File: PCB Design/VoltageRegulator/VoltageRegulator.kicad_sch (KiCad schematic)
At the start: 31 parts, among them J1 Screw_Terminal_01x08, J2 SMA, J3 SMA, J4 SMA, J5 SMA, J6 SMA, J7 SMA, J8 Screw_Terminal_01x01, U1 LM7815_TO220, U2 L7805, U3 ADL5902ACPZ-R7, U4 LM358

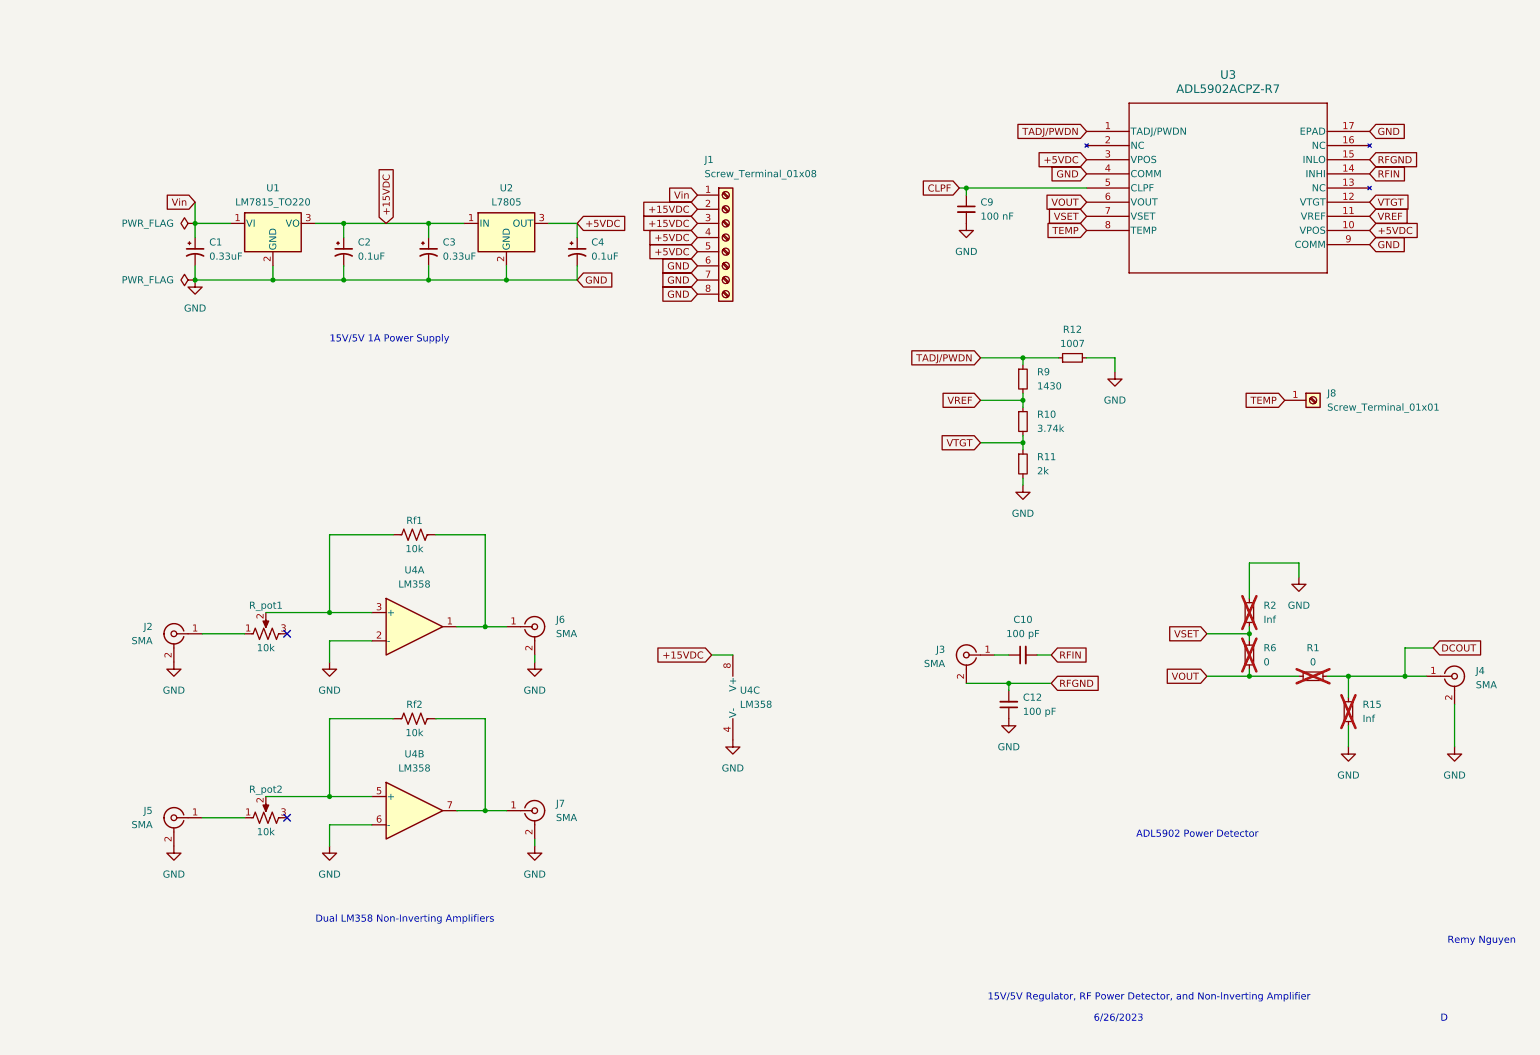
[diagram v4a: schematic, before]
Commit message: New circuit diagram  with current draw
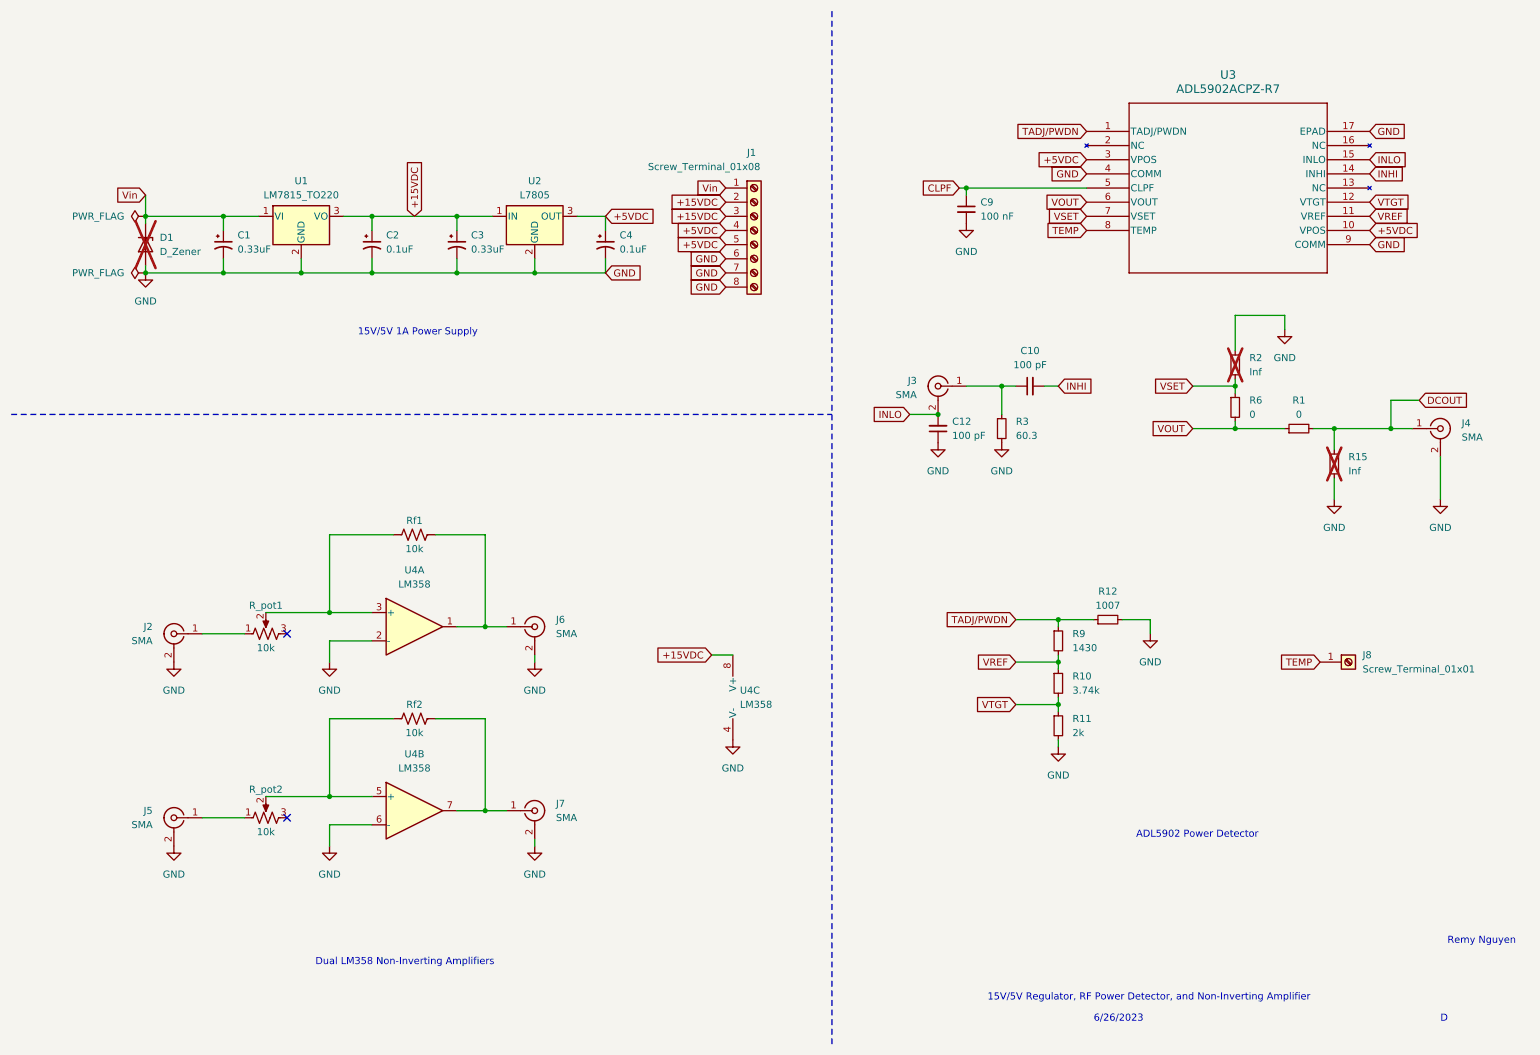
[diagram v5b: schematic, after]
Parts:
- added D1: D_Zener, symbol Device:D_Zener
- added R3: 60.3, symbol Device:R_Small
- R1, R6: now fitted
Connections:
- net GND: now also D1.2 (A), R3.2
- net Vin: now also D1.1 (K)
- net at C10.1, J3.1 (In): now also R3.1
- net RFGND renamed INLO
- net RFIN renamed INHI
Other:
- moved on the sheet: C1, C10, C12, C2, C3, C4, J1, J3, J4, J8, R10, R11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

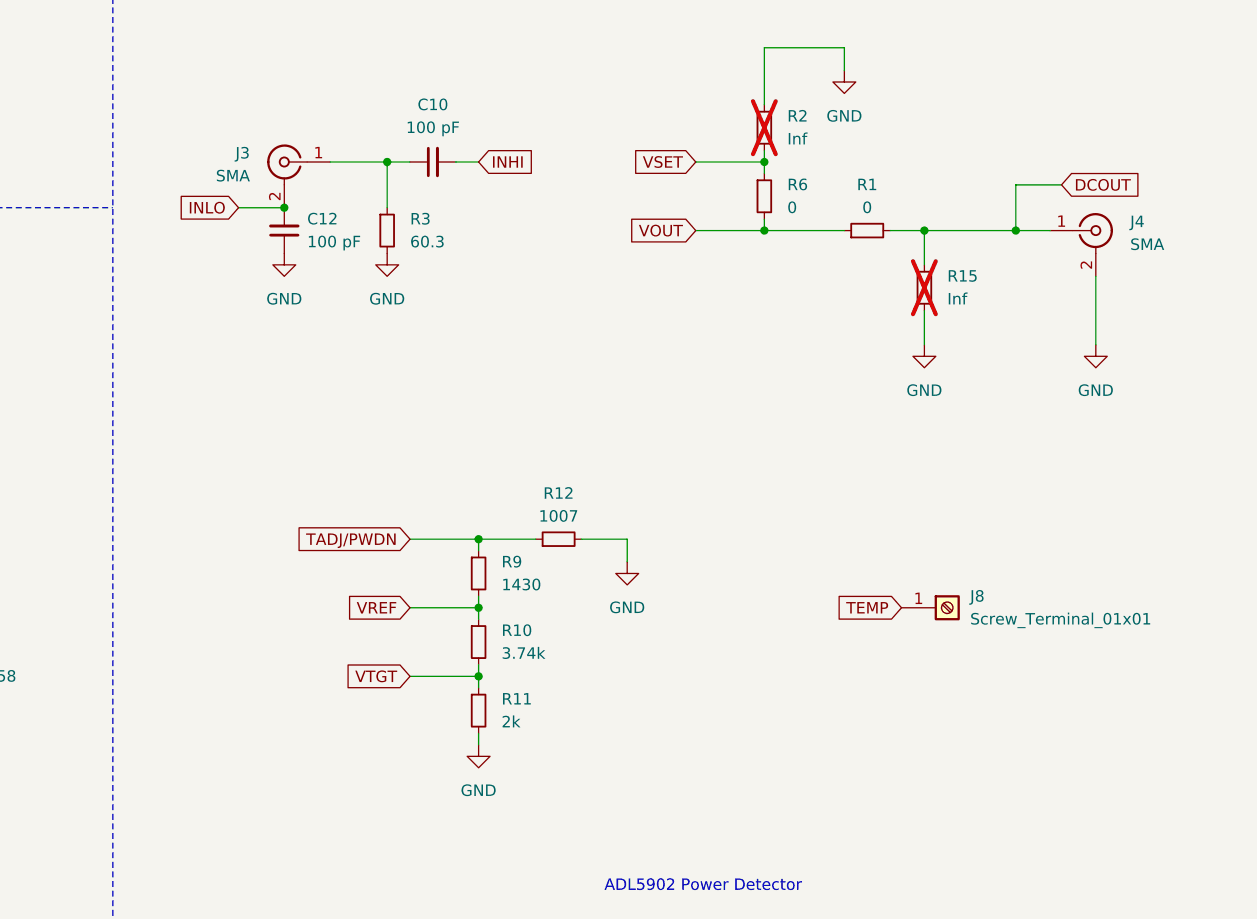
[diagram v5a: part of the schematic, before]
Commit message: INLO fixed; INLO is unused differential input, not RFGND
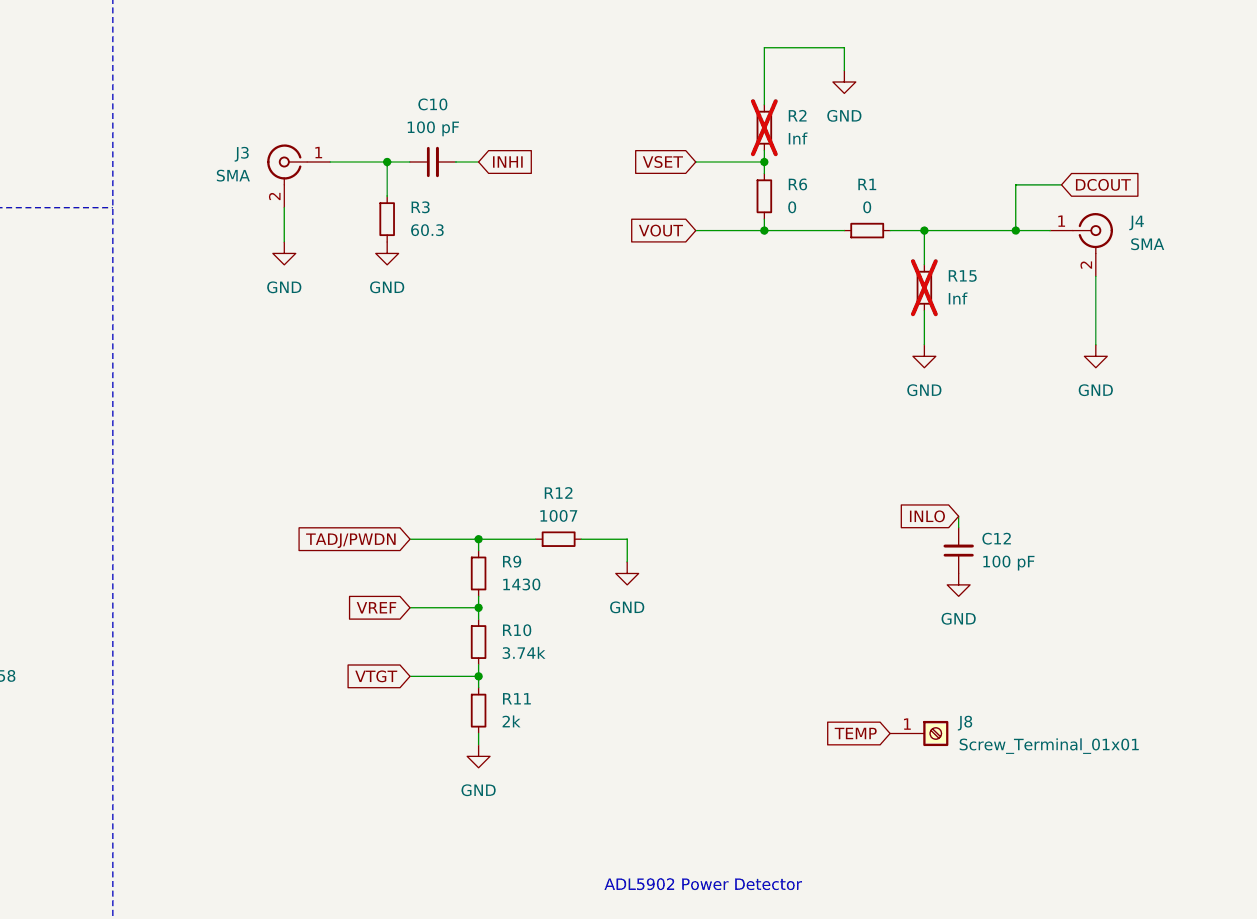
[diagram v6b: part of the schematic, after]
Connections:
- net GND: now also J3.2 (Ext)
- net INLO: no longer J3.2 (Ext)
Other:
- moved on the sheet: C12, J8, R3
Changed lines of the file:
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@@
   (junction (at 232.41 87.63) (diameter 0) (color 0 0 0 0)
-  )
-  (junction (at 179.07 85.09) (diameter 0) (color 0 0 0 0)
   )
   (junction (at 200.66 137.16) (diameter 0) (color 0 0 0 0)
@@
     (stroke (width 0) (type default))
   )
+  (wire (pts (xy 179.07 85.09) (xy 179.07 88.9))
+    (stroke (width 0) (type default))
+  )
   (wire (pts (xy 97.79 139.7) (xy 88.9 139.7))
     (stroke (width 0) (type default))
@@
     (stroke (width 0) (type default))
   )
-  (wire (pts (xy 190.5 80.01) (xy 190.5 85.09))
+  (wire (pts (xy 190.5 80.01) (xy 190.5 83.82))
     (stroke (width 0) (type default))
   )
@@
     (stroke (width 0) (type default))
   )
-  (wire (pts (xy 173.99 85.09) (xy 179.07 85.09))
+  (wire (pts (xy 254 119.38) (xy 254 120.65))
     (stroke (width 0) (type default))
   )
@@
     )
   )
-  (global_label "INLO" (shape input) (at 173.99 85.09 180) (fields_autoplaced)
-    (effects (font (size 1.27 1.27)) (justify right))
-    (property "Intersheetrefs" "${INTERSHEET_REFS}" (at 166.7903 85.09 0)
+  (global_label "INLO" (shape input) (at 254 119.38 180) (fields_autoplaced)
+    (effects (font (size 1.27 1.27)) (justify right))
+    (property "Intersheetrefs" "${INTERSHEET_REFS}" (at 246.8003 119.38 0)
       (effects (font (size 1.27 1.27)) (justify right) hide)
     )
@@
     )
   )
-  (global_label "TEMP" (shape input) (at 247.65 129.54 180) (fields_autoplaced)
-    (effects (font (size 1.27 1.27)) (justify right))
-    (property "Intersheetrefs" "${INTERSHEET_REFS}" (at 239.9062 129.54 0)
+  (global_label "TEMP" (shape input) (at 246.38 143.51 180) (fields_autoplaced)
+    (effects (font (size 1.27 1.27)) (justify right))
+    (property "Intersheetrefs" "${INTERSHEET_REFS}" (at 238.6362 143.51 0)
       (effects (font (size 1.27 1.27)) (justify right) hide)
     )
@@
     )
   )
-  (symbol (lib_id "Device:R_Small") (at 190.5 87.63 0) (unit 1)
-    (in_bom yes) (on_board yes) (dnp no) (fields_autoplaced)
-    (property "Reference" "R3" (at 193.04 86.36 0)
-      (effects (font (size 1.27 1.27)) (justify left))
-    )
-    (property "Value" "60.3" (at 193.04 88.9 0)
-      (effects (font (size 1.27 1.27)) (justify left))
-    )
-    (property "Footprint" "" (at 190.5 87.63 0)
-      (effects (font (size 1.27 1.27)) hide)
-    )
-    (property "Datasheet" "~" (at 190.5 87.63 0)
+  (symbol (lib_id "Device:R_Small") (at 190.5 86.36 0) (unit 1)
+    (in_bom yes) (on_board yes) (dnp no) (fields_autoplaced)
+    (property "Reference" "R3" (at 193.04 85.09 0)
+      (effects (font (size 1.27 1.27)) (justify left))
+    )
+    (property "Value" "60.3" (at 193.04 87.63 0)
+      (effects (font (size 1.27 1.27)) (justify left))
+    )
+    (property "Footprint" "" (at 190.5 86.36 0)
+      (effects (font (size 1.27 1.27)) hide)
+    )
+    (property "Datasheet" "~" (at 190.5 86.36 0)
       (effects (font (size 1.27 1.27)) hide)
     )
@@
     )
   )
+  (symbol (lib_id "power:GND") (at 179.07 88.9 0) (unit 1)
+    (in_bom yes) (on_board yes) (dnp no) (fields_autoplaced)
+    (property "Reference" "#PWR03" (at 179.07 95.25 0)
+      (effects (font (size 1.27 1.27)) hide)
+    )
+    (property "Value" "GND" (at 179.07 93.98 0)
+      (effects (font (size 1.27 1.27)))
+    )
+    (property "Footprint" "" (at 179.07 88.9 0)
+      (effects (font (size 1.27 1.27)) hide)
+    )
+    (property "Datasheet" "" (at 179.07 88.9 0)
+      (effects (font (size 1.27 1.27)) hide)
+    )
+    (pin "1")
+    (instances
+      (project "VoltageRegulator"
+        (path "/0e389307-4ee7-48a5-9908-22ab90894211"
+          (reference "#PWR03") (unit 1)
+        )
+      )
+    )
+  )
   (symbol (lib_id "power:GND") (at 217.17 124.46 0) (unit 1)
     (in_bom yes) (on_board yes) (dnp no) (fields_autoplaced)
@@
     )
   )
-  (symbol (lib_id "Connector:Screw_Terminal_01x01") (at 252.73 129.54 0) (unit 1)
-    (in_bom yes) (on_board yes) (dnp no) (fields_autoplaced)
-    (property "Reference" "J8" (at 255.27 128.27 0)
-      (effects (font (size 1.27 1.27)) (justify left))
-    )
-    (property "Value" "Screw_Terminal_01x01" (at 255.27 130.81 0)
-      (effects (font (size 1.27 1.27)) (justify left))
-    )
-    (property "Footprint" "" (at 252.73 129.54 0)
-      (effects (font (size 1.27 1.27)) hide)
-    )
-    (property "Datasheet" "~" (at 252.73 129.54 0)
+  (symbol (lib_id "Connector:Screw_Terminal_01x01") (at 251.46 143.51 0) (unit 1)
+    (in_bom yes) (on_board yes) (dnp no) (fields_autoplaced)
+    (property "Reference" "J8" (at 254 142.24 0)
+      (effects (font (size 1.27 1.27)) (justify left))
+    )
+    (property "Value" "Screw_Terminal_01x01" (at 254 144.78 0)
+      (effects (font (size 1.27 1.27)) (justify left))
+    )
+    (property "Footprint" "" (at 251.46 143.51 0)
+      (effects (font (size 1.27 1.27)) hide)
+    )
+    (property "Datasheet" "~" (at 251.46 143.51 0)
       (effects (font (size 1.27 1.27)) hide)
     )
@@
     )
   )
-  (symbol (lib_id "power:GND") (at 190.5 90.17 0) (unit 1)
-    (in_bom yes) (on_board yes) (dnp no) (fields_autoplaced)
-    (property "Reference" "#PWR02" (at 190.5 96.52 0)
-      (effects (font (size 1.27 1.27)) hide)
-    )
-    (property "Value" "GND" (at 190.5 95.25 0)
-      (effects (font (size 1.27 1.27)))
-    )
-    (property "Footprint" "" (at 190.5 90.17 0)
-      (effects (font (size 1.27 1.27)) hide)
-    )
-    (property "Datasheet" "" (at 190.5 90.17 0)
+  (symbol (lib_id "power:GND") (at 190.5 88.9 0) (unit 1)
+    (in_bom yes) (on_board yes) (dnp no) (fields_autoplaced)
+    (property "Reference" "#PWR02" (at 190.5 95.25 0)
+      (effects (font (size 1.27 1.27)) hide)
+    )
+    (property "Value" "GND" (at 190.5 93.98 0)
+      (effects (font (size 1.27 1.27)))
+    )
+    (property "Footprint" "" (at 190.5 88.9 0)
+      (effects (font (size 1.27 1.27)) hide)
+    )
+    (property "Datasheet" "" (at 190.5 88.9 0)
       (effects (font (size 1.27 1.27)) hide)
     )
@@
     )
   )
-  (symbol (lib_id "power:GND") (at 179.07 90.17 0) (unit 1)
-    (in_bom yes) (on_board yes) (dnp no) (fields_autoplaced)
-    (property "Reference" "#PWR011" (at 179.07 96.52 0)
-      (effects (font (size 1.27 1.27)) hide)
-    )
-    (property "Value" "GND" (at 179.07 95.25 0)
-      (effects (font (size 1.27 1.27)))
-    )
-    (property "Footprint" "" (at 179.07 90.17 0)
-      (effects (font (size 1.27 1.27)) hide)
-    )
-    (property "Datasheet" "" (at 179.07 90.17 0)
+  (symbol (lib_id "power:GND") (at 254 125.73 0) (unit 1)
+    (in_bom yes) (on_board yes) (dnp no) (fields_autoplaced)
+    (property "Reference" "#PWR011" (at 254 132.08 0)
+      (effects (font (size 1.27 1.27)) hide)
+    )
+    (property "Value" "GND" (at 254 130.81 0)
+      (effects (font (size 1.27 1.27)))
+    )
+    (property "Footprint" "" (at 254 125.73 0)
+      (effects (font (size 1.27 1.27)) hide)
+    )
+    (property "Datasheet" "" (at 254 125.73 0)
       (effects (font (size 1.27 1.27)) hide)
     )
@@
     )
   )
-  (symbol (lib_id "Device:C_Small") (at 179.07 87.63 180) (unit 1)
-    (in_bom yes) (on_board yes) (dnp no) (fields_autoplaced)
-    (property "Reference" "C12" (at 181.61 86.3536 0)
+  (symbol (lib_id "Device:C_Small") (at 254 123.19 180) (unit 1)
+    (in_bom yes) (on_board yes) (dnp no) (fields_autoplaced)
+    (property "Reference" "C12" (at 256.54 121.9136 0)
       (effects (font (size 1.27 1.27)) (justify right))
     )
-    (property "Value" "100 pF" (at 181.61 88.8936 0)
+    (property "Value" "100 pF" (at 256.54 124.4536 0)
       (effects (font (size 1.27 1.27)) (justify right))
     )
-    (property "Footprint" "" (at 179.07 87.63 0)
-      (effects (font (size 1.27 1.27)) hide)
-    )
-    (property "Datasheet" "~" (at 179.07 87.63 0)
-      (effects (font (size 1.27 1.27)) hide)
-    )
+    (property "Footprint" "" (at 254 123.19 0)
+      (effects (font (size 1.27 1.27)) hide)
+    )
+    (property "Datasheet" "~" (at 254 123.19 0)
+      (effects (font (size 1.27 1.27)) hide)
+    )

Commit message: Footprints assigned, LM7815 --> L7815
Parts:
- C1, C2, C3, C4: footprint Capacitor_THT:CP_Radial_Tantal_D4.5mm_P2.50mm -> Capacitor_Tantalum_SMD:CP_EIA-1608-08_AVX-J
- C10, C12: footprint (none) -> Capacitor_SMD:C_1206_3216Metric
- C9: footprint (none) -> Capacitor_SMD:C_0805_2012Metric
- D1: footprint (none) -> Diode_SMD:D_1206_3216Metric
- J2, J3, J4, J5, J6, J7: footprint (none) -> Connector_Coaxial:SMA_Molex_73251-1153_EdgeMount_Horizontal
- J8: value Screw_Terminal_01x01 -> Conn_01x01; footprint (none) -> Connector_PinHeader_1.00mm:PinHeader_1x01_P1.00mm_Vertical; symbol Connector:Screw_Terminal_01x01 -> Connector_Generic:Conn_01x01; now not fitted
- R1, R12, R15, R2, R6, R9, Rf1, Rf2: footprint (none) -> Resistor_SMD:R_1206_3216Metric
- R10, R11, R3: footprint (none) -> Resistor_SMD:R_0805_2012Metric
- R_pot1, R_pot2: footprint (none) -> Potentiometer_THT:Potentiometer_Bourns_3006P_Horizontal
- U1: value LM7815_TO220 -> L7815; symbol Regulator_Linear:LM7815_TO220 -> Regulator_Linear:L7815
- U2: footprint (none) -> Package_TO_SOT_THT:TO-220-3_Horizontal_TabDown
- U3: footprint CP_16_20_ADI -> imports:CP_16_20_ADI
- U4: footprint (none) -> Package_DIP:DIP-8_W7.62mm
